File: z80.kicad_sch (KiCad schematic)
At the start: 44 parts, among them IC4 Z80CPU, IC5 LC3664, IC901 TL974

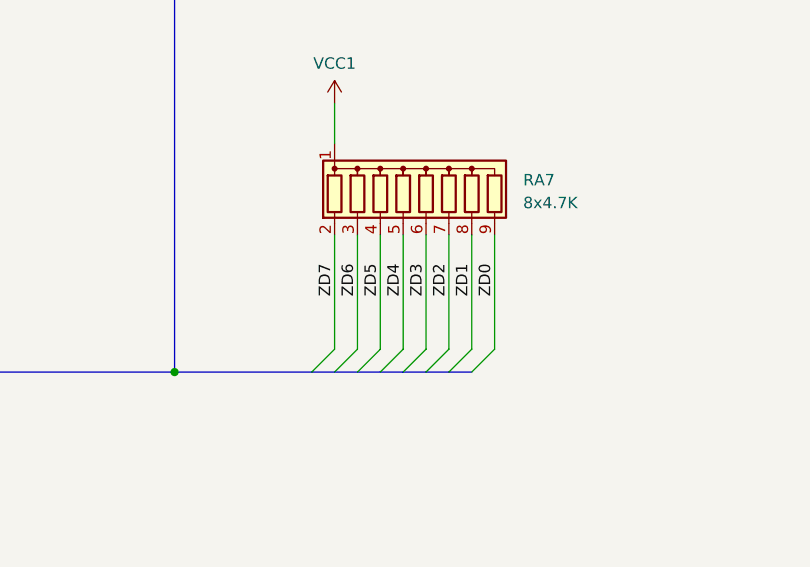
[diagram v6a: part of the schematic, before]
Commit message: Figure out clearances.
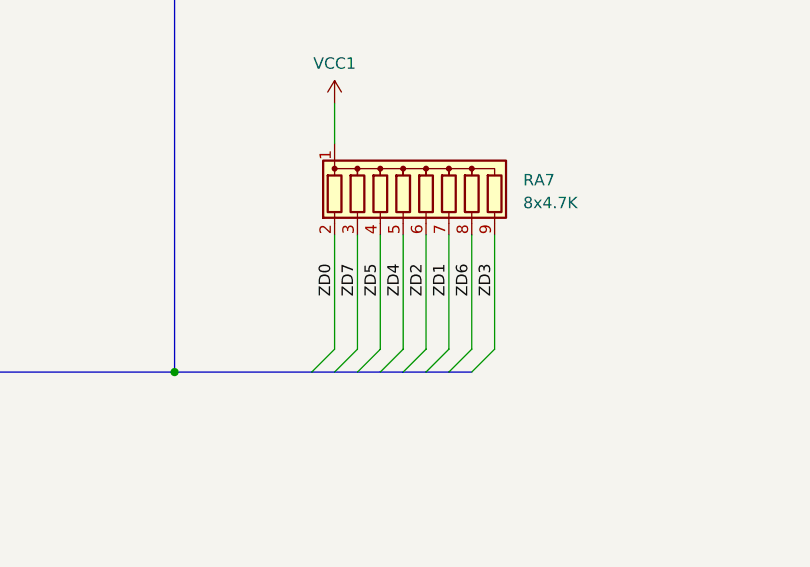
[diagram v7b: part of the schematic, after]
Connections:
- net ZD0: now also RA7.2 (R1); no longer RA7.9 (R8)
- net ZD1: now also RA7.7 (R6); no longer RA7.8 (R7)
- net ZD2: now also RA7.6 (R5); no longer RA7.7 (R6)
- net ZD3: now also RA7.9 (R8); no longer RA7.6 (R5)
- net ZD6: now also RA7.8 (R7); no longer RA7.3 (R2)
- net ZD7: now also RA7.3 (R2); no longer RA7.2 (R1)
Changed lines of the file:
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@@
     (effects (font (size 2.54 2.54)) (justify left bottom))
   )
-  (label "ZD6" (at 212.09 117.475 270) (fields_autoplaced)
+  (label "ZD6" (at 224.79 117.475 270) (fields_autoplaced)
     (effects (font (size 1.27 1.27)) (justify right bottom))
   )
@@
     (effects (font (size 1.27 1.27)) (justify left bottom))
   )
-  (label "ZD7" (at 209.55 117.475 270) (fields_autoplaced)
+  (label "ZD7" (at 212.09 117.475 270) (fields_autoplaced)
     (effects (font (size 1.27 1.27)) (justify right bottom))
   )
@@
     (effects (font (size 1.27 1.27)) (justify left bottom))
   )
-  (label "ZD3" (at 219.71 117.475 270) (fields_autoplaced)
+  (label "ZD3" (at 227.33 117.475 270) (fields_autoplaced)
     (effects (font (size 1.27 1.27)) (justify right bottom))
   )
@@
     (effects (font (size 1.27 1.27)) (justify left bottom))
   )
-  (label "ZD1" (at 224.79 117.475 270) (fields_autoplaced)
+  (label "ZD1" (at 222.25 117.475 270) (fields_autoplaced)
     (effects (font (size 1.27 1.27)) (justify right bottom))
   )
@@
     (effects (font (size 1.27 1.27)) (justify left bottom))
   )
-  (label "ZD0" (at 227.33 117.475 270) (fields_autoplaced)
+  (label "ZD0" (at 209.55 117.475 270) (fields_autoplaced)
     (effects (font (size 1.27 1.27)) (justify right bottom))
   )
@@
     (effects (font (size 1.27 1.27)) (justify right bottom))
   )
-  (label "ZD2" (at 222.25 117.475 270) (fields_autoplaced)
+  (label "ZD2" (at 219.71 117.475 270) (fields_autoplaced)
     (effects (font (size 1.27 1.27)) (justify right bottom))
   )

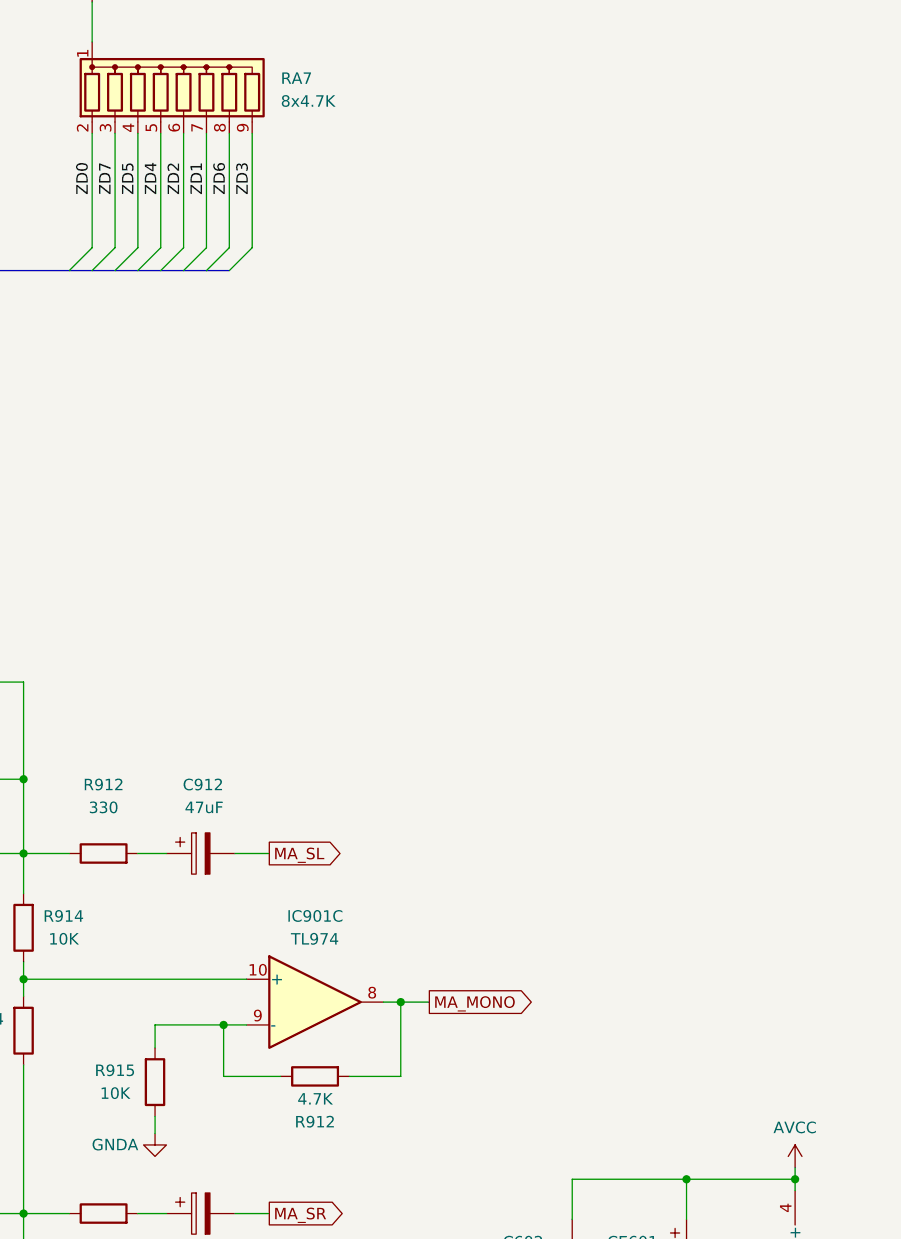
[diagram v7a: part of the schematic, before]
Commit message: Place remaining passives.
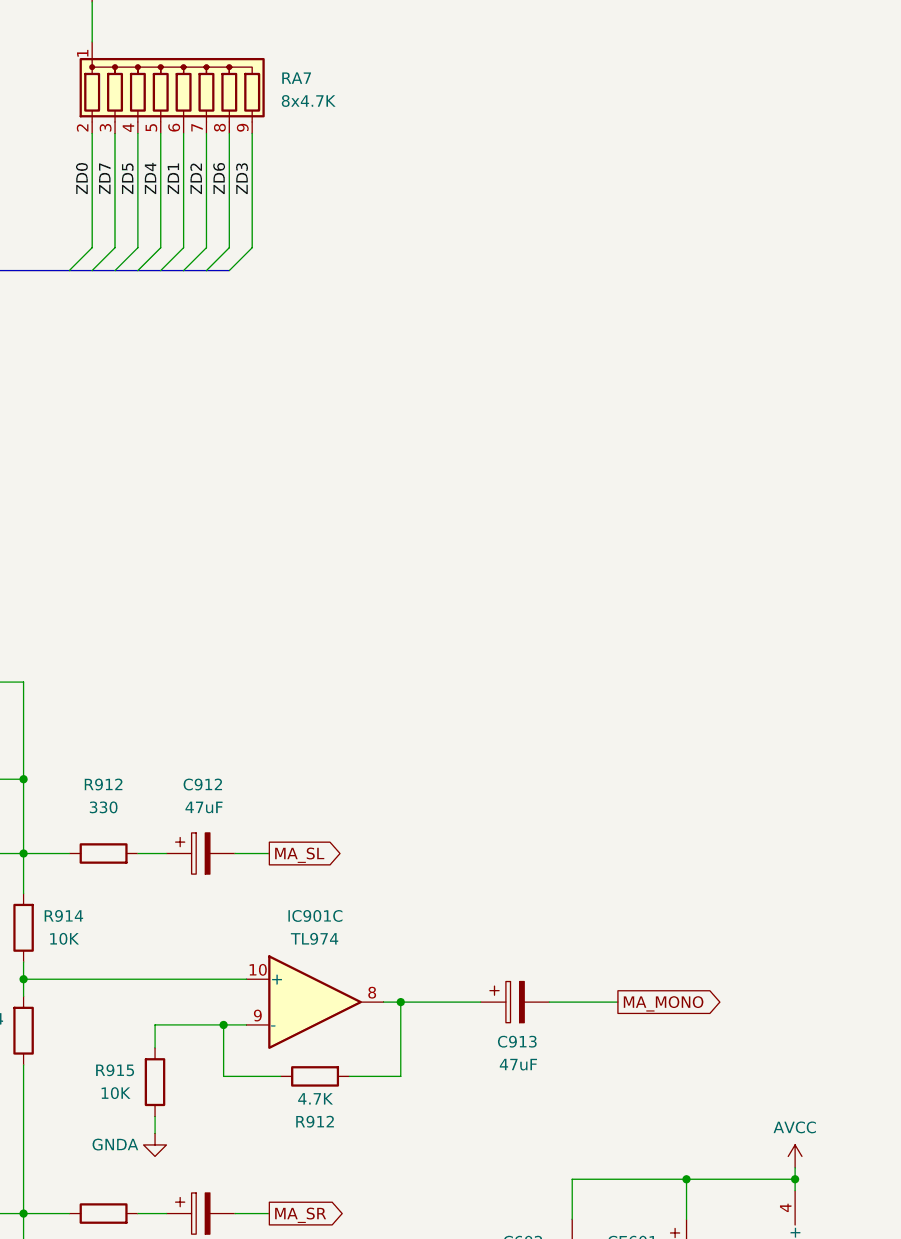
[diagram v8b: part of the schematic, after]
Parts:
- added C913: 47uF, Capacitor_THT:CP_Radial_D5.0mm_P2.50mm, symbol Device:C_Polarized
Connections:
- net MA_MONO: now also C913.2; no longer IC901.8, R912.2
- net ZD1: now also RA7.6 (R5); no longer RA7.7 (R6)
- net ZD2: now also RA7.7 (R6); no longer RA7.6 (R5)
- new net: C913.1, IC901.8, R912.2
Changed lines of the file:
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@@
+    (stroke (width 0) (type default))
+  )
+  (wire (pts (xy 260.35 210.82) (xy 267.97 210.82))
     (stroke (width 0) (type default))
   )
@@
     (stroke (width 0) (type default))
   )
-  (wire (pts (xy 243.84 210.82) (xy 247.015 210.82))
+  (wire (pts (xy 243.84 210.82) (xy 252.73 210.82))
     (stroke (width 0) (type default))
   )
@@
     (effects (font (size 1.27 1.27)) (justify left bottom))
   )
-  (label "ZD1" (at 222.25 117.475 270) (fields_autoplaced)
+  (label "ZD1" (at 219.71 117.475 270) (fields_autoplaced)
     (effects (font (size 1.27 1.27)) (justify right bottom))
   )
@@
     (effects (font (size 1.27 1.27)) (justify right bottom))
   )
-  (label "ZD2" (at 219.71 117.475 270) (fields_autoplaced)
+  (label "ZD2" (at 222.25 117.475 270) (fields_autoplaced)
     (effects (font (size 1.27 1.27)) (justify right bottom))
   )
@@
     )
   )
-  (global_label "MA_MONO" (shape output) (at 247.015 210.82 0) (fields_autoplaced)
+  (global_label "MA_MONO" (shape output) (at 267.97 210.82 0) (fields_autoplaced)
     (effects (font (size 1.27 1.27)) (justify left))
-    (property "Intersheetrefs" "${INTERSHEET_REFS}" (at 258.9507 210.82 0)
+    (property "Intersheetrefs" "${INTERSHEET_REFS}" (at 279.9057 210.82 0)
       (effects (font (size 1.27 1.27)) (justify left) hide)
     )
@@
         )
       )
+    )
+  )
+  (symbol (lib_id "Device:C_Polarized") (at 256.54 210.82 90) (mirror x) (unit 1)
+    (in_bom yes) (on_board yes) (dnp no)
+    (property "Reference" "C913" (at 259.08 215.265 90)
+      (effects (font (size 1.27 1.27)) (justify left))
+    )
+    (property "Value" "47uF" (at 259.08 217.805 90)
+      (effects (font (size 1.27 1.27)) (justify left))
+    )
+    (property "Footprint" "Capacitor_THT:CP_Radial_D5.0mm_P2.50mm" (at 260.35 211.7852 0)
+      (effects (font (size 1.27 1.27)) hide)
+    )
+    (property "Datasheet" "~" (at 256.54 210.82 0)
+      (effects (font (size 1.27 1.27)) hide)
+    )
+    (pin "1")
+    (pin "2")
+    (instances
+      (project "Neptune"
+        (path "/bcc23b51-b742-4ae5-9dd6-d96a24058944/01513199-62c5-4123-a151-ccd381a5e6c1"
+          (reference "C913") (unit 1)
+        )
+        (path "/bcc23b51-b742-4ae5-9dd6-d96a24058944/293c8f1f-2c58-4557-aeb8-8502bb66fbd4"
+          (reference "CE915") (unit 1)
+        )
+      )
